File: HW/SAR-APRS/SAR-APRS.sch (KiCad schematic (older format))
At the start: 1 part

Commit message: update
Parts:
- added U?: DRA818V, symbol APRS_modules:DRA818V
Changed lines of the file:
@@
 EESchema Schematic File Version 4
+LIBS:SAR-APRS-cache
 EELAYER 26 0
 EELAYER END
@@
 L modules:Arduino_Nano_v3.x A1
 U 1 1 5BAE34B2
-P 5825 3550
-F 0 "A1" H 5825 2464 50  0000 C CNN
-F 1 "Arduino_Nano_v3.x" H 5825 2373 50  0000 C CNN
-F 2 "Modules:Arduino_Nano" H 5975 2600 50  0001 L CNN
-F 3 "http://www.mouser.com/pdfdocs/Gravitech_Arduino_Nano3_0.pdf" H 5825 2550 50  0001 C CNN
-	1    5825 3550
+P 5850 5025
+F 0 "A1" H 5850 3939 50  0000 C CNN
+F 1 "Arduino_Nano_v3.x" H 5850 3848 50  0000 C CNN
+F 2 "Modules:Arduino_Nano" H 6000 4075 50  0001 L CNN
+F 3 "http://www.mouser.com/pdfdocs/Gravitech_Arduino_Nano3_0.pdf" H 5850 4025 50  0001 C CNN
+	1    5850 5025
 	1    0    0    -1
 $EndComp
+$Comp
+L APRS_modules:DRA818V U?
+U 1 1 5BAE857D
+P 7800 3250
+F 0 "U?" H 8328 3296 50  0000 L CNN
+F 1 "DRA818V" H 8328 3205 50  0000 L CNB
+F 2 "" H 7150 3600 50  0001 C CNN
+F 3 "" H 7150 3600 50  0001 C CNN
+	1    7800 3250
+	1    0    0    -1
+$EndComp
+Entry Wire Line
+	7300 6950 7400 7050
+Entry Wire Line
+	7300 6950 7400 7050
+Entry Wire Line
+	7300 6950 7400 7050
+Entry Wire Line
+	7300 6950 7400 7050
+Entry Wire Line
+	7300 6950 7400 7050
+Entry Wire Line
+	7300 6950 7400 7050
+Entry Wire Line
+	7300 6950 7400 7050
+Entry Wire Line
+	7300 6950 7400 7050
+Entry Wire Line
+	7300 6950 7400 7050
+Entry Wire Line
+	7300 6950 7400 7050
+Entry Wire Line
+	7300 6950 7400 7050
+Entry Wire Line
+	7300 6950 7400 7050
+Entry Wire Line
+	7300 6950 7400 7050
+Entry Wire Line
+	7300 6950 7400 7050
+Entry Wire Line
+	7300 6950 7400 7050
+Entry Wire Line
+	7300 6950 7400 7050
+Entry Wire Line
+	7300 6950 7400 7050
+Entry Wire Line
+	7300 6950 7400 7050
+Entry Wire Line
+	10300 6000 10400 6100
+Entry Wire Line
+	10300 6000 10400 6100
+Entry Wire Line
+	10350 6000 10450 6100
 $EndSCHEMATC

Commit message: update
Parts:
- removed A1: Arduino_Nano_v3.x, Modules:Arduino_Nano, symbol modules:Arduino_Nano_v3.x
- added U2: arduino_mini_clone, APRS_modules:arduino_mini_clone, symbol APRS_modules:arduino_mini_clone
- U1: renamed from U?; footprint (none) -> APRS_modules:DRA818
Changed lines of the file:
@@
 $EndDescr
 $Comp
-L modules:Arduino_Nano_v3.x A1
-U 1 1 5BAE34B2
-P 5850 5025
-F 0 "A1" H 5850 3939 50  0000 C CNN
-F 1 "Arduino_Nano_v3.x" H 5850 3848 50  0000 C CNN
-F 2 "Modules:Arduino_Nano" H 6000 4075 50  0001 L CNN
-F 3 "http://www.mouser.com/pdfdocs/Gravitech_Arduino_Nano3_0.pdf" H 5850 4025 50  0001 C CNN
-	1    5850 5025
-	1    0    0    -1
-$EndComp
-$Comp
-L APRS_modules:DRA818V U?
+L APRS_modules:DRA818V U1
 U 1 1 5BAE857D
 P 7800 3250
-F 0 "U?" H 8328 3296 50  0000 L CNN
-F 1 "DRA818V" H 8328 3205 50  0000 L CNB
-F 2 "" H 7150 3600 50  0001 C CNN
+F 0 "U1" H 7325 3600 50  0000 L CNN
+F 1 "DRA818V" H 7525 3250 50  0000 L CNN
+F 2 "APRS_modules:DRA818" H 7150 3600 50  0001 C CNN
 F 3 "" H 7150 3600 50  0001 C CNN
 	1    7800 3250
 	1    0    0    -1
 $EndComp
-Entry Wire Line
-	7300 6950 7400 7050
-Entry Wire Line
-	7300 6950 7400 7050
-Entry Wire Line
-	7300 6950 7400 7050
-Entry Wire Line
-	7300 6950 7400 7050
-Entry Wire Line
-	7300 6950 7400 7050
-Entry Wire Line
-	7300 6950 7400 7050
-Entry Wire Line
-	7300 6950 7400 7050
-Entry Wire Line
-	7300 6950 7400 7050
-Entry Wire Line
-	7300 6950 7400 7050
-Entry Wire Line
-	7300 6950 7400 7050
-Entry Wire Line
-	7300 6950 7400 7050
-Entry Wire Line
-	7300 6950 7400 7050
-Entry Wire Line
-	7300 6950 7400 7050
-Entry Wire Line
-	7300 6950 7400 7050
-Entry Wire Line
-	7300 6950 7400 7050
-Entry Wire Line
-	7300 6950 7400 7050
-Entry Wire Line
-	7300 6950 7400 7050
-Entry Wire Line
-	7300 6950 7400 7050
-Entry Wire Line
-	10300 6000 10400 6100
-Entry Wire Line
-	10300 6000 10400 6100
-Entry Wire Line
-	10350 6000 10450 6100
+$Comp
+L APRS_modules:arduino_mini_clone U2
+U 1 1 5BB140ED
+P 4675 3300
+F 0 "U2" H 3950 3700 50  0000 R CNN
+F 1 "arduino_mini_clone" H 5025 3325 50  0000 R CNN
+F 2 "APRS_modules:arduino_mini_clone" H 3775 3450 50  0001 C CNN
+F 3 "" H 3775 3450 50  0001 C CNN
+	1    4675 3300
+	1    0    0    -1
+$EndComp
 $EndSCHEMATC

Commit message: update
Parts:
- added U3: ATMEGA328P-MMH, Housings_DFN_QFN:QFN-28-1EP_4x4mm_Pitch0.4mm, symbol atmel:ATMEGA328P-MMH
- added U?: FT230XQ, QFN-16, symbol ftdi:FT230XQ
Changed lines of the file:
@@
+	1    0    0    -1
+$EndComp
+$Comp
+L atmel:ATMEGA328P-MMH U3
+U 1 1 5BDFFC65
+P 2200 4575
+F 0 "U3" H 2250 5942 50  0000 C CNN
+F 1 "ATMEGA328P-MMH" H 2250 5851 50  0000 C CNN
+F 2 "Housings_DFN_QFN:QFN-28-1EP_4x4mm_Pitch0.4mm" H 2200 4575 50  0001 C CIN
+F 3 "http://www.atmel.com/images/atmel-8271-8-bit-avr-microcontroller-atmega48a-48pa-88a-88pa-168a-168pa-328-328p_datasheet.pdf" H 2200 4575 50  0001 C CNN
+	1    2200 4575
+	1    0    0    -1
+$EndComp
+$Comp
+L ftdi:FT230XQ U?
+U 1 1 5BDFFE23
+P 5100 5075
+F 0 "U?" H 5100 5953 50  0000 C CNN
+F 1 "FT230XQ" H 5100 5862 50  0000 C CNN
+F 2 "QFN-16" H 5100 5075 50  0001 C CNN
+F 3 "http://www.ftdichip.com/Products/ICs/FT230X.html" H 5100 5075 50  0001 C CNN
+	1    5100 5075
 	1    0    0    -1
 $EndComp

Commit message: update
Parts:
- removed U3: ATMEGA328P-MMH, Housings_DFN_QFN:QFN-28-1EP_4x4mm_Pitch0.4mm, symbol atmel:ATMEGA328P-MMH
- removed U?: FT230XQ, QFN-16, symbol ftdi:FT230XQ
- added C? (x4): C_Small, symbol device:C_Small
- added J1, J?: uFl, w_conn_rf:coaxial_u.fl-r-smt-1, symbol Connector:Conn_Coaxial
- added L1, L? (x3): L_Small, symbol device:L_Small
- added R1: R_Small, symbol device:R_Small
- added U3: NEO-M8, symbol APRS_modules:NEO-M8
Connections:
- net labels added: GND
- wire segments 0 -> 26
- no-connect marks 0 -> 1
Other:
- moved on the sheet: U1, U2

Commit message: update
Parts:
- added Q?: 2N7002, TO_SOT_Packages_SMD:SOT-23, symbol Transistor:2N7002
- added RV1: 100k, symbol device:R_POT
- C? (x2): value C_Small -> 20pF
- C? (x2): value C_Small -> 36pF
- L? (x2): value L_Small -> 56nH
- L?: value L_Small -> 68nH
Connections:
- net GND: now also U1.P2, U1.P3, Q?.2 (S), RV1.1; no longer U1.8 (VBAT)
- net at U1.18 (MIC_IN): now also RV1.3
- net at U1.5 (PTT): now also Q?.3 (D)
- no-connect marks 1 -> 2
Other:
- moved on the sheet: R1
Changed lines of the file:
@@
 L device:R_Small R1
 U 1 1 5BDAC67E
-P 2400 3000
-F 0 "R1" V 2204 3000 50  0000 C CNN
-F 1 "R_Small" V 2295 3000 50  0000 C CNN
-F 2 "" H 2400 3000 50  0001 C CNN
-F 3 "~" H 2400 3000 50  0001 C CNN
-	1    2400 3000
+P 2250 2950
+F 0 "R1" V 2054 2950 50  0000 C CNN
+F 1 "R_Small" V 2145 2950 50  0000 C CNN
+F 2 "" H 2250 2950 50  0001 C CNN
+F 3 "~" H 2250 2950 50  0001 C CNN
+	1    2250 2950
 	0    1    1    0
 $EndComp
-Wire Wire Line
-	2500 3000 2750 3000
-Wire Wire Line
-	2300 3000 2200 3000
-Wire Wire Line
-	2200 3000 2200 2950
-Wire Wire Line
-	2200 2950 2000 2950
 $Comp
 L device:L_Small L?
@@
 P 2600 4850
 F 0 "L?" V 2785 4850 50  0000 C CNN
-F 1 "L_Small" V 2694 4850 50  0000 C CNN
+F 1 "56nH" V 2694 4850 50  0000 C CNN
 F 2 "" H 2600 4850 50  0001 C CNN
 F 3 "~" H 2600 4850 50  0001 C CNN
@@
 P 2200 4850
 F 0 "L?" V 2385 4850 50  0000 C CNN
-F 1 "L_Small" V 2294 4850 50  0000 C CNN
+F 1 "68nH" V 2294 4850 50  0000 C CNN
 F 2 "" H 2200 4850 50  0001 C CNN
 F 3 "~" H 2200 4850 50  0001 C CNN
@@
 P 1800 4850
 F 0 "L?" V 1985 4850 50  0000 C CNN
-F 1 "L_Small" V 1894 4850 50  0000 C CNN
+F 1 "56nH" V 1894 4850 50  0000 C CNN
 F 2 "" H 1800 4850 50  0001 C CNN
 F 3 "~" H 1800 4850 50  0001 C CNN
@@
 P 1600 5050
 F 0 "C?" H 1692 5096 50  0000 L CNN
-F 1 "C_Small" H 1692 5005 50  0000 L CNN
+F 1 "20pF" H 1692 5005 50  0000 L CNN
 F 2 "" H 1600 5050 50  0001 C CNN
 F 3 "~" H 1600 5050 50  0001 C CNN
@@
 P 2000 5050
 F 0 "C?" H 2092 5096 50  0000 L CNN
-F 1 "C_Small" H 2092 5005 50  0000 L CNN
+F 1 "36pF" H 2092 5005 50  0000 L CNN
 F 2 "" H 2000 5050 50  0001 C CNN
 F 3 "~" H 2000 5050 50  0001 C CNN
@@
 P 2400 5050
 F 0 "C?" H 2492 5096 50  0000 L CNN
-F 1 "C_Small" H 2492 5005 50  0000 L CNN
+F 1 "36pF" H 2492 5005 50  0000 L CNN
 F 2 "" H 2400 5050 50  0001 C CNN
 F 3 "~" H 2400 5050 50  0001 C CNN
@@
 P 2800 5050
 F 0 "C?" H 2892 5096 50  0000 L CNN
-F 1 "C_Small" H 2892 5005 50  0000 L CNN
+F 1 "20pF" H 2892 5005 50  0000 L CNN
 F 2 "" H 2800 5050 50  0001 C CNN
 F 3 "~" H 2800 5050 50  0001 C CNN
@@
 	3050 5600 3050 5700
 Wire Wire Line
-	3050 5800 3150 5800
-Wire Wire Line
 	3150 5700 3050 5700
 Connection ~ 3050 5700
 Wire Wire Line
-	3050 5700 3050 5800
-Wire Wire Line
 	3000 5700 3050 5700
 NoConn ~ 3150 5500
+$Comp
+L Transistor:2N7002 Q?
+U 1 1 5BDD44C9
+P 3850 6450
+F 0 "Q?" H 4056 6496 50  0000 L CNN
+F 1 "2N7002" H 4056 6405 50  0000 L CNN
+F 2 "TO_SOT_Packages_SMD:SOT-23" H 4050 6375 50  0001 L CIN
+F 3 "https://www.fairchildsemi.com/datasheets/2N/2N7002.pdf" H 3850 6450 50  0001 L CNN
+	1    3850 6450
+	-1   0    0    -1
+$EndComp
+Wire Wire Line
+	3750 6050 3750 6250
+$Comp
+L power:GND #PWR?
+U 1 1 5BDD8B35
+P 3750 6650
+F 0 "#PWR?" H 3750 6400 50  0001 C CNN
+F 1 "GND" V 3755 6522 50  0000 R CNN
+F 2 "" H 3750 6650 50  0001 C CNN
+F 3 "" H 3750 6650 50  0001 C CNN
+	1    3750 6650
+	1    0    0    -1
+$EndComp
+NoConn ~ 3550 6050
+$Comp
+L device:R_POT RV1
+U 1 1 5BDDDD1E
+P 4150 4900
+F 0 "RV1" H 4400 5150 50  0000 R CNN
+F 1 "100k" H 4450 5050 50  0000 R CNN
+F 2 "" H 4150 4900 50  0001 C CNN
+F 3 "~" H 4150 4900 50  0001 C CNN
+	1    4150 4900
+	1    0    0    -1
+$EndComp
+Wire Wire Line
+	4150 5050 4150 5250
+$Comp
+L power:GND #PWR?
+U 1 1 5BDE2374
+P 4150 4650
+F 0 "#PWR?" H 4150 4400 50  0001 C CNN
+F 1 "GND" V 4155 4522 50  0000 R CNN
+F 2 "" H 4150 4650 50  0001 C CNN
+F 3 "" H 4150 4650 50  0001 C CNN
+	1    4150 4650
+	-1   0    0    1
+$EndComp
+Wire Wire Line
+	4150 4650 4150 4750
+Wire Wire Line
+	2000 2950 2150 2950
+Wire Wire Line
+	2350 2950 2500 2950
+Wire Wire Line
+	2500 2950 2500 3000
+Wire Wire Line
+	2500 3000 2750 3000
+$Comp
+L power:GND #PWR?
+U 1 1 5BDF2B36
+P 4450 5900
+F 0 "#PWR?" H 4450 5650 50  0001 C CNN
+F 1 "GND" V 4455 5772 50  0000 R CNN
+F 2 "" H 4450 5900 50  0001 C CNN
+F 3 "" H 4450 5900 50  0001 C CNN
+	1    4450 5900
+	1    0    0    -1
+$EndComp
+Wire Wire Line
+	4400 5650 4450 5650
+Wire Wire Line
+	4450 5650 4450 5800
+Wire Wire Line
+	4400 5800 4450 5800
+Connection ~ 4450 5800
+Wire Wire Line
+	4450 5800 4450 5900
 $EndSCHEMATC

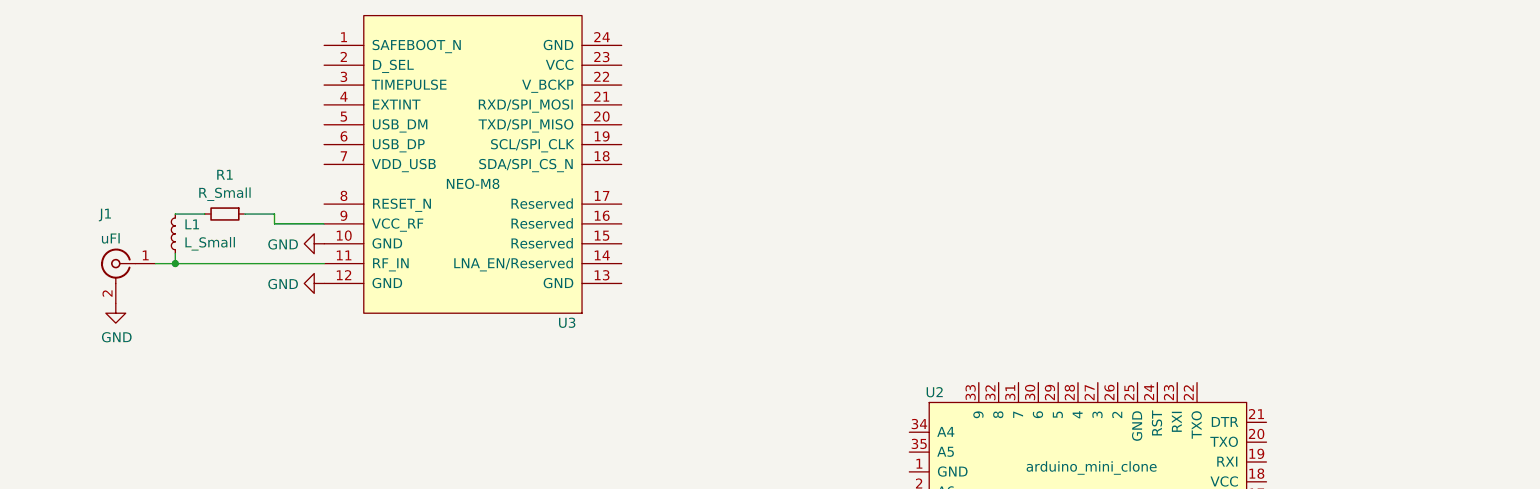
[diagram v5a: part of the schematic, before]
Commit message: schematic update
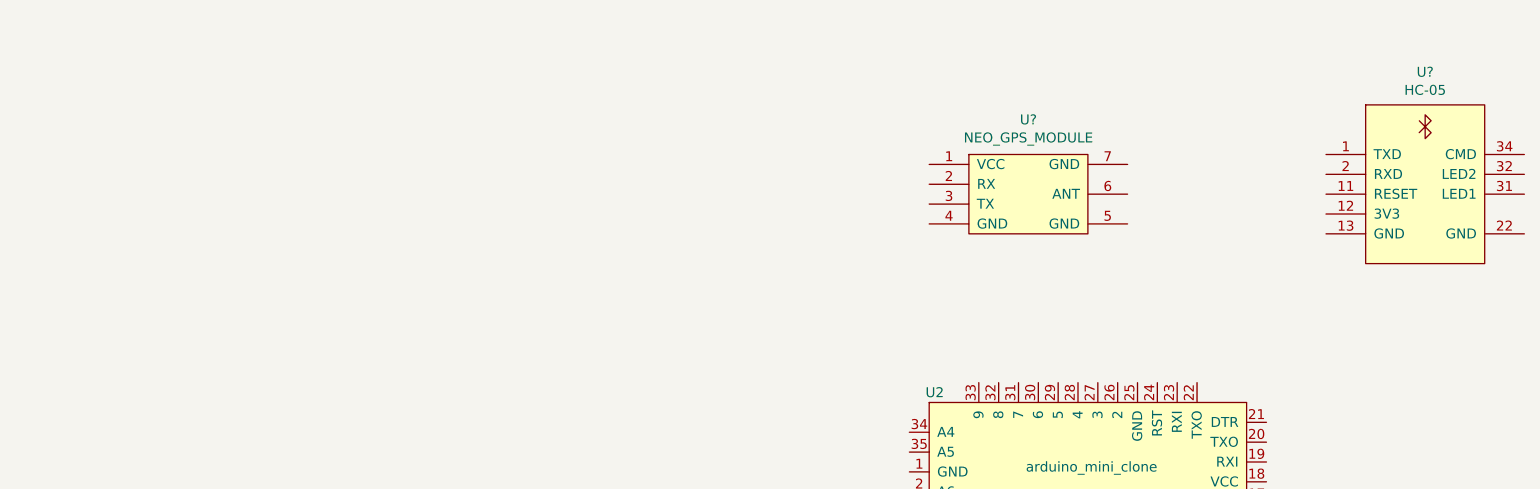
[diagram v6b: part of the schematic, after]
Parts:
- removed J1: uFl, w_conn_rf:coaxial_u.fl-r-smt-1, symbol Connector:Conn_Coaxial
- removed L1: L_Small, symbol device:L_Small
- removed R1: R_Small, symbol device:R_Small
- removed U3: NEO-M8, symbol APRS_modules:NEO-M8
- added U?: HC-05, symbol APRS_modules:HC-05
- added U?: NEO_GPS_MODULE, symbol APRS_modules:NEO_GPS_MODULE
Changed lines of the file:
@@
-$EndComp
-$Comp
-L APRS_modules:NEO-M8 U3
-U 1 1 5BD8DBF8
-P 3500 2700
-F 0 "U3" H 3025 3500 50  0000 C CNN
-F 1 "NEO-M8" H 3500 2800 50  0000 C CNN
-F 2 "" H 3050 3800 50  0001 C CNN
-F 3 "" H 3050 3800 50  0001 C CNN
-	1    3500 2700
-	-1   0    0    1
-$EndComp
-$Comp
-L Connector:Conn_Coaxial J1
-U 1 1 5BDA4D58
-P 1700 3200
-F 0 "J1" H 1750 3450 50  0000 C CNN
-F 1 "uFl" H 1725 3325 50  0000 C CNN
-F 2 "w_conn_rf:coaxial_u.fl-r-smt-1" H 1700 3200 50  0001 C CNN
-F 3 " ~" H 1700 3200 50  0001 C CNN
-	1    1700 3200
-	-1   0    0    -1
-$EndComp
-Wire Wire Line
-	1900 3200 2000 3200
-$Comp
-L power:GND #PWR0101
-U 1 1 5BDA6514
-P 1700 3400
-F 0 "#PWR0101" H 1700 3150 50  0001 C CNN
-F 1 "GND" H 1705 3227 50  0000 C CNN
-F 2 "" H 1700 3400 50  0001 C CNN
-F 3 "" H 1700 3400 50  0001 C CNN
-	1    1700 3400
-	1    0    0    -1
-$EndComp
-$Comp
-L power:GND #PWR0102
-U 1 1 5BDA6B19
-P 2750 3300
-F 0 "#PWR0102" H 2750 3050 50  0001 C CNN
-F 1 "GND" V 2755 3172 50  0000 R CNN
-F 2 "" H 2750 3300 50  0001 C CNN
-F 3 "" H 2750 3300 50  0001 C CNN
-	1    2750 3300
-	0    1    1    0
-$EndComp
-$Comp
-L power:GND #PWR0103
-U 1 1 5BDA733A
-P 2750 3100
-F 0 "#PWR0103" H 2750 2850 50  0001 C CNN
-F 1 "GND" V 2755 2972 50  0000 R CNN
-F 2 "" H 2750 3100 50  0001 C CNN
-F 3 "" H 2750 3100 50  0001 C CNN
-	1    2750 3100
-	0    1    1    0
-$EndComp
-$Comp
-L device:L_Small L1
-U 1 1 5BDA902B
-P 2000 3050
-F 0 "L1" H 1956 3004 50  0000 R CNN
-F 1 "L_Small" H 1956 3095 50  0000 R CNN
-F 2 "" H 2000 3050 50  0001 C CNN
-F 3 "~" H 2000 3050 50  0001 C CNN
-	1    2000 3050
-	-1   0    0    1
-$EndComp
-Wire Wire Line
-	2000 3150 2000 3200
-Connection ~ 2000 3200
-Wire Wire Line
-	2000 3200 2750 3200
-$Comp
-L device:R_Small R1
-U 1 1 5BDAC67E
-P 2250 2950
-F 0 "R1" V 2054 2950 50  0000 C CNN
-F 1 "R_Small" V 2145 2950 50  0000 C CNN
-F 2 "" H 2250 2950 50  0001 C CNN
-F 3 "~" H 2250 2950 50  0001 C CNN
-	1    2250 2950
-	0    1    1    0
 $EndComp
 $Comp
@@
 Wire Wire Line
 	4150 4650 4150 4750
-Wire Wire Line
-	2000 2950 2150 2950
-Wire Wire Line
-	2350 2950 2500 2950
-Wire Wire Line
-	2500 2950 2500 3000
-Wire Wire Line
-	2500 3000 2750 3000
 $Comp
 L power:GND #PWR?
@@
 Wire Wire Line
 	4450 5800 4450 5900
+$Comp
+L APRS_modules:NEO_GPS_MODULE U?
+U 1 1 5BF7E675
+P 6300 2850
+F 0 "U?" H 6300 3225 50  0000 C CNN
+F 1 "NEO_GPS_MODULE" H 6300 3134 50  0000 C CNN
+F 2 "" H 5800 3150 50  0001 C CNN
+F 3 "" H 5800 3150 50  0001 C CNN
+	1    6300 2850
+	1    0    0    -1
+$EndComp
+$Comp
+L APRS_modules:HC-05 U?
+U 1 1 5BF7514D
+P 8300 2850
+F 0 "U?" H 8300 3465 50  0000 C CNN
+F 1 "HC-05" H 8300 3374 50  0000 C CNN
+F 2 "" H 7800 3200 50  0001 C CNN
+F 3 "" H 7800 3200 50  0001 C CNN
+	1    8300 2850
+	1    0    0    -1
+$EndComp
 $EndSCHEMATC
